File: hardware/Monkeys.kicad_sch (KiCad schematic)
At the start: 141 parts, among them IC1 SI4702-C19-GM, J1 JTAG, J2 3.3vSerial, J3 Therm, J4 PJ-320D-4A, J5 10118194-0001LF, Q1 BSS138, Q2 SI2302, Q3 MMBT3904, Q4 MMBT3904, Q5 MMBT3904, Q6 MMBT3904, SW1 SW_Push, SW2 SW_Push, SW3 SW_Push, SW4 SW_Push, SW5 SPDT_Switch_Grounded, U1 BQ24072RGT, U2 RT9080-33GJ5, U3 CH340C, U4 LM4808, U5 InfraredReceiver, U6 ESP32-WROOM-32E(8MB), Y1 32.768KHZ, Y2 32.768KHZ

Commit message: hardware: Badge revision 3.4
After a holiday break work on revision 3.4 of the Monkey badge began
March 24th, 2023.

In this revision changes were made to the following components:
- power regulator
- Charge/powerpath controller
- the headphone jack
- Resistor/capacitor values on the LM4808 amplifer
- Removal of experimental touch pads

This spin of the hardware went to initial manufacturing with the gerbers
provided on July 25th, 2023.
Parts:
- removed C13: 10uF, monkeys20221112:C_0603_1608Metric, symbol Device:C_Small
- removed CT1, CT2, CT3, CT4: Touchpad, JTFooties:CAPSENSE-CIRCLE-D10MM, symbol JTFooties2:Touchpad
- removed JP1: RESET, monkeys20221112:SolderJumper-2_P1.3mm_Open_RoundedPad1.0x1.5mm, symbol Jumper:SolderJumper_2_Open
- removed JP4: RBypassA, monkeys20221112:SolderJumper-3_P1.3mm_Bridged12_RoundedPad1.0x1.5mm, symbol Jumper:SolderJumper_3_Bridged12
- removed JP5: LBypass2, monkeys20221112:SolderJumper-3_P1.3mm_Bridged12_RoundedPad1.0x1.5mm, symbol Jumper:SolderJumper_3_Bridged12
- removed JP6: RBypassB, monkeys20221112:SolderJumper-3_P1.3mm_Bridged12_RoundedPad1.0x1.5mm, symbol Jumper:SolderJumper_3_Bridged12
- removed JP7: Amp Power Disable, monkeys20221112:SolderJumper-2_P1.3mm_Bridged_RoundedPad1.0x1.5mm, symbol Jumper:SolderJumper_2_Bridged
- added C10: 10uF, monkeys20221112:C_0603_1608Metric, symbol Device:C_Small
- added C11: 100uF, monkeys20221112:CP_EIA-6032-20_AVX-F, symbol Device:C_Polarized_Small
- added C13, C16: 330uF, Capacitor_Tantalum_SMD:CP_EIA-7343-31_Kemet-D, symbol Device:C_Polarized
- added D12: Green, monkeys20221112:LED_0805_2012Metric, symbol Device:LED
- added FB1, FB2: SCBG100505U801T, Inductor_SMD:L_0402_1005Metric, symbol Device:FerriteBead_Small
- added JP1: EXT Therm, Jumper:SolderJumper-2_P1.3mm_Bridged_RoundedPad1.0x1.5mm, symbol Jumper:SolderJumper_2_Bridged
- added JP2: ANT/GNDA, Jumper:SolderJumper-3_P1.3mm_Bridged12_RoundedPad1.0x1.5mm, symbol Jumper:SolderJumper_3_Bridged12
- added L4: 22uH, Inductor_SMD:L_Bourns-SRN4018, symbol Device:L_Ferrite
- added R37: 10K, monkeys20221112:R_0402_1005Metric, symbol Device:R_Small
- added SW6: SW_MEC_5E, JTFooties:Button_metal, symbol Switch:SW_MEC_5E
- added SW7: SPDT_Switch, monkeys20221112:SPDT Switch MSK12C02-HB, symbol JTFooties2:SPDT_Switch_Grounded
- added U7: Boost5V, Package_TO_SOT_SMD:SOT-23-5, symbol JTFooties2:ME2188C33M5
- AE1, AE2, BT2, DRA1, H1, H2, HS1, J1, J2, J3, JP12, JP13, JP14, JP15, R25, R32, R35, SAO1, SAO2, TP1: JLCPCB Part #（optional) (none) -> DNP
- BT1: footprint monkeys20221112:1xAA -> JTFooties:1xAA_NUB; JLCPCB Part #（optional) (none) -> DNP
- C15: value 10uF -> 100pF; footprint monkeys20221112:C_0603_1608Metric -> Capacitor_SMD:C_0402_1005Metric; JLCPCB Part #（optional) C326057 -> C1546; Manufacturer_Part_Number CC0603KRX5R6BB106 -> 0402CG101J500NT; SeeedSKU 302010103 -> (none); price .02 -> (none)
- C29, C30: JLCPCB Part #（optional) C109462 -> C2835558; Manufacturer_Part_Number CC0805MKX5R5BB226 -> C0805X6S226M6R3NT
- C8, C9: value 1uF -> 390nF; JLCPCB Part #（optional) C106254 -> C350937; Manufacturer_Part_Number CC0402KRX5R6BB105 -> GRM155R61A394KE15D
- D11: JLCPCB Part #（optional) C73929 -> C2764887; Manufacturer_Part_Number IR26-21C/L110/TR8 -> MHT153IRCT
- JP10: value MIC/GND -> MIC/GNDA; JLCPCB Part #（optional) (none) -> DNP
- JP3: value LBypass1 -> PWMLOUT; JLCPCB Part #（optional) (none) -> DNP
- JP9: value GND/MIC -> GNDA/MIC; JLCPCB Part #（optional) (none) -> DNP
- L1: JLCPCB Part #（optional) C408752 -> C341697; Manufacturer_Part_Number SDWL1608CR12JSTFM01 -> LQW18ANR12J00D
- LCD1: footprint monkeys20221112:PinHeader_1x04_P2.54mm_Vertical -> Connector_PinHeader_2.54mm:PinHeader_1x04_P2.54mm_Vertical; JLCPCB Part #（optional) (none) -> DNP
- R14, R16: value 3.9K -> 20K; JLCPCB Part #（optional) C51721 -> C25765; Manufacturer_Part_Number 0402WGF3901TCE -> 0402WGF2002TCE
- R17, R18: value 3.9K -> 30K; JLCPCB Part #（optional) C51721 -> C138008; Manufacturer_Part_Number 0402WGF3901TCE -> RC0402FR-0730KL
- R5: value 46.4K -> 1K; footprint monkeys20221112:R_0402_1005Metric -> monkeys20221112:R_0805_2012Metric; JLCPCB Part #（optional) C227093 -> C100046; Manufacturer_Part_Number AC0402FR-0746K4L -> RC0805JR-071KL; SeeedSKU AC0402FR-0746K4L -> 301010311
- SW5: value SPDT_Switch_Grounded -> SPDT_Switch
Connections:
- net LBP is gone; now on net PWMLOUT: JP3.3 (B)
- net +3V3: now also JP12.3 (B), JP13.1 (A), R5.2; no longer JP12.1 (A), JP13.3 (B)
- net +VDC: now also SW7.2; no longer R4.2, R6.2, U1.5 (EN2)
- net BATT: now also R32.1 (A)
- net GND: now also JP12.1 (A), JP13.3 (B), U1.14 (TMR), C10.1, C11.2, D12.1 (K), R37.1, SW6.1, SW6.2, SW7.4, U7.4 (GND); no longer JP12.3 (B), JP13.1 (A), R5.1
- net GNDA: now also JP2.3 (B); no longer JP10.1 (A), JP9.3 (B)
- net LAUD: now also C13.2, FB2.2
- net MIC: now also JP10.1 (A), JP9.3 (B); no longer JP10.3 (B), JP9.1 (A)
- net RAUD: now also C16.2, FB1.1; no longer C15.2
- net ROUT: now also C9.2
- net RST: now also SW6.3 (K), SW6.4 (A)
- net THERM: now also JP1.1 (A)
- net +5V: now reaches C7.2, R23.1, U4.8 (V+)
- net +5V: now also C11.1, U7.1 (CE), U7.2 (VOUT)
- net at R11.2, R17.1, U4.7: now also C13.1
- net at J4.R1: now also FB1.2
- net at J4.T: now also FB2.1
- net FMIP: now reaches AE1.1 (A), IC1.2 (FMIP), L1.2, TP1.1
- net FMIP: now also C15.1
- net at R15.2, R18.1, U4.1: now also C16.1; no longer C15.1
- net IO26_INFRARCV renamed PWMLOUT
- net POUT renamed OUT
- net OUT: now also R4.2, R6.2, U1.5 (EN2); no longer R32.1 (A)
- new net: D12.2 (A), R5.1
- new net: JP10.3 (B), JP2.2 (C), JP9.1 (A)
- new net: L4.1, SW7.1 (ON)
- new net: C10.2, L4.2, U7.5 (LX)
- new net: C15.2, JP2.1 (A)
- new net: JP1.2 (B), R37.2
- no-connect marks 24 -> 25
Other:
- note added: "Cb"
- note added: "Charge, Powerpath Coontroller & On/Off Switch"
- note added: "Ci"
- note added: "Co"
- note added: "Cs"
- note added: "Cut if using ext therm"
- note added: "External NTC 10k 1% Thermistor on battery"
- note added: "Rf"
- note added: "Ri"
- note added: "https://www.alibaba.com/product-detail/14500-Rechargeable-Battery-AA-2800mAh-3_1600779695589.html?spm=a2700.galleryofferlist.normal_offer.d_title.a7ed2679IqySss"
- note added: "https://www.alibaba.com/product-detail/Gaonengmax-3-7V-14500-1200mah-li_1600451606725.html?spm=a2700.galleryofferlist.normal_offer.d_title.1a322679m4llBO"
- note added: "https://www.alibaba.com/product-detail/Rechargeable-Cylinder-14500-1200mAh-Lithium-Battery_1600453629274.html?spm=a2700.galleryofferlist.normal_offer.d_title.1a322679m4llBO"
- note removed: "32mA"
- note removed: "46.4K R5 = 6.25Hr Limit on charge"
- note removed: "Charge & Powerpath Controller"
- note removed: "Experimental Alternative to physical buttons"
- note removed: "External 10k 1% Thermistor on battery"
- note removed: "two 1UF caps in series, close enough to 2.2uF"
- moved on the sheet: C27, D10, D9, JP10, JP12, JP13, JP14, JP15, JP9, R17, R18, R4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

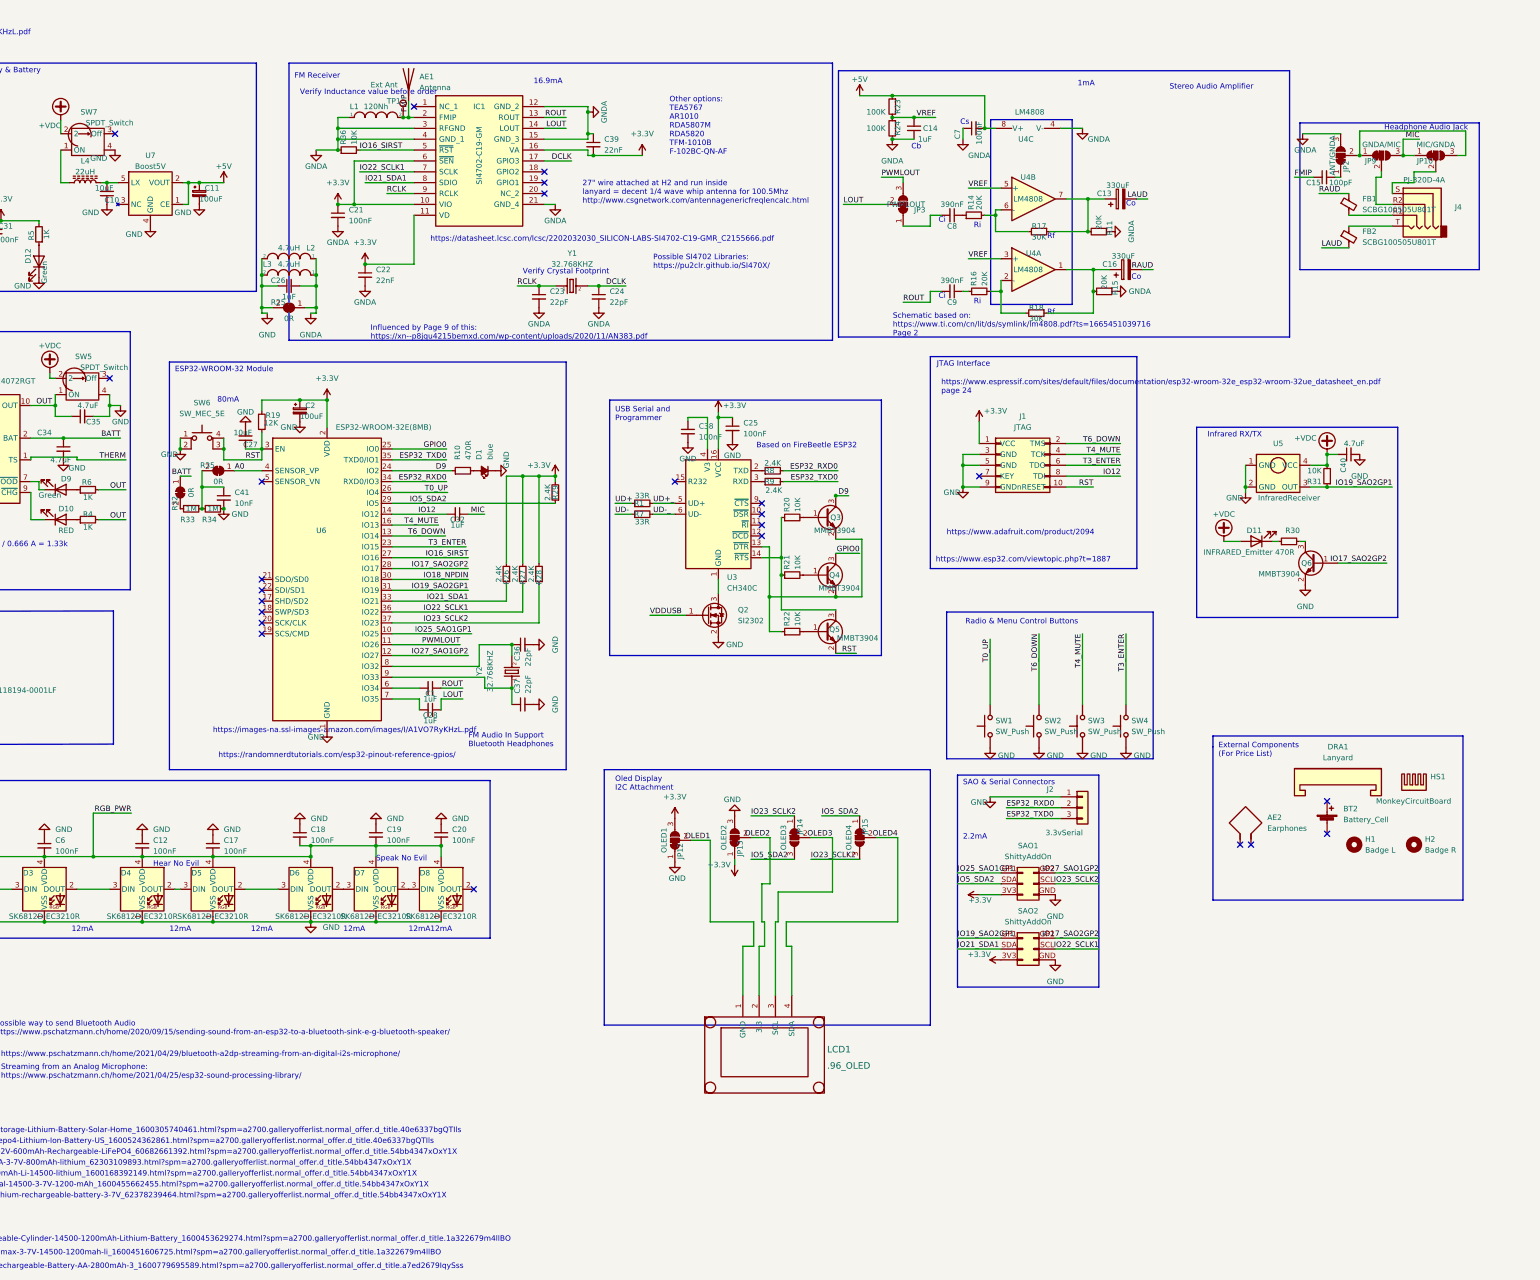
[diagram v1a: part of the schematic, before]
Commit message: hardware: Badge revision 3.5
In this revision changes were made to the following components:

- Stereo amplifier
- Microphone amplifier
- Addition of a JTAG port

This spin of the hardware went to initial manufacturing with the gerbers
provided on August 30th, 2023.
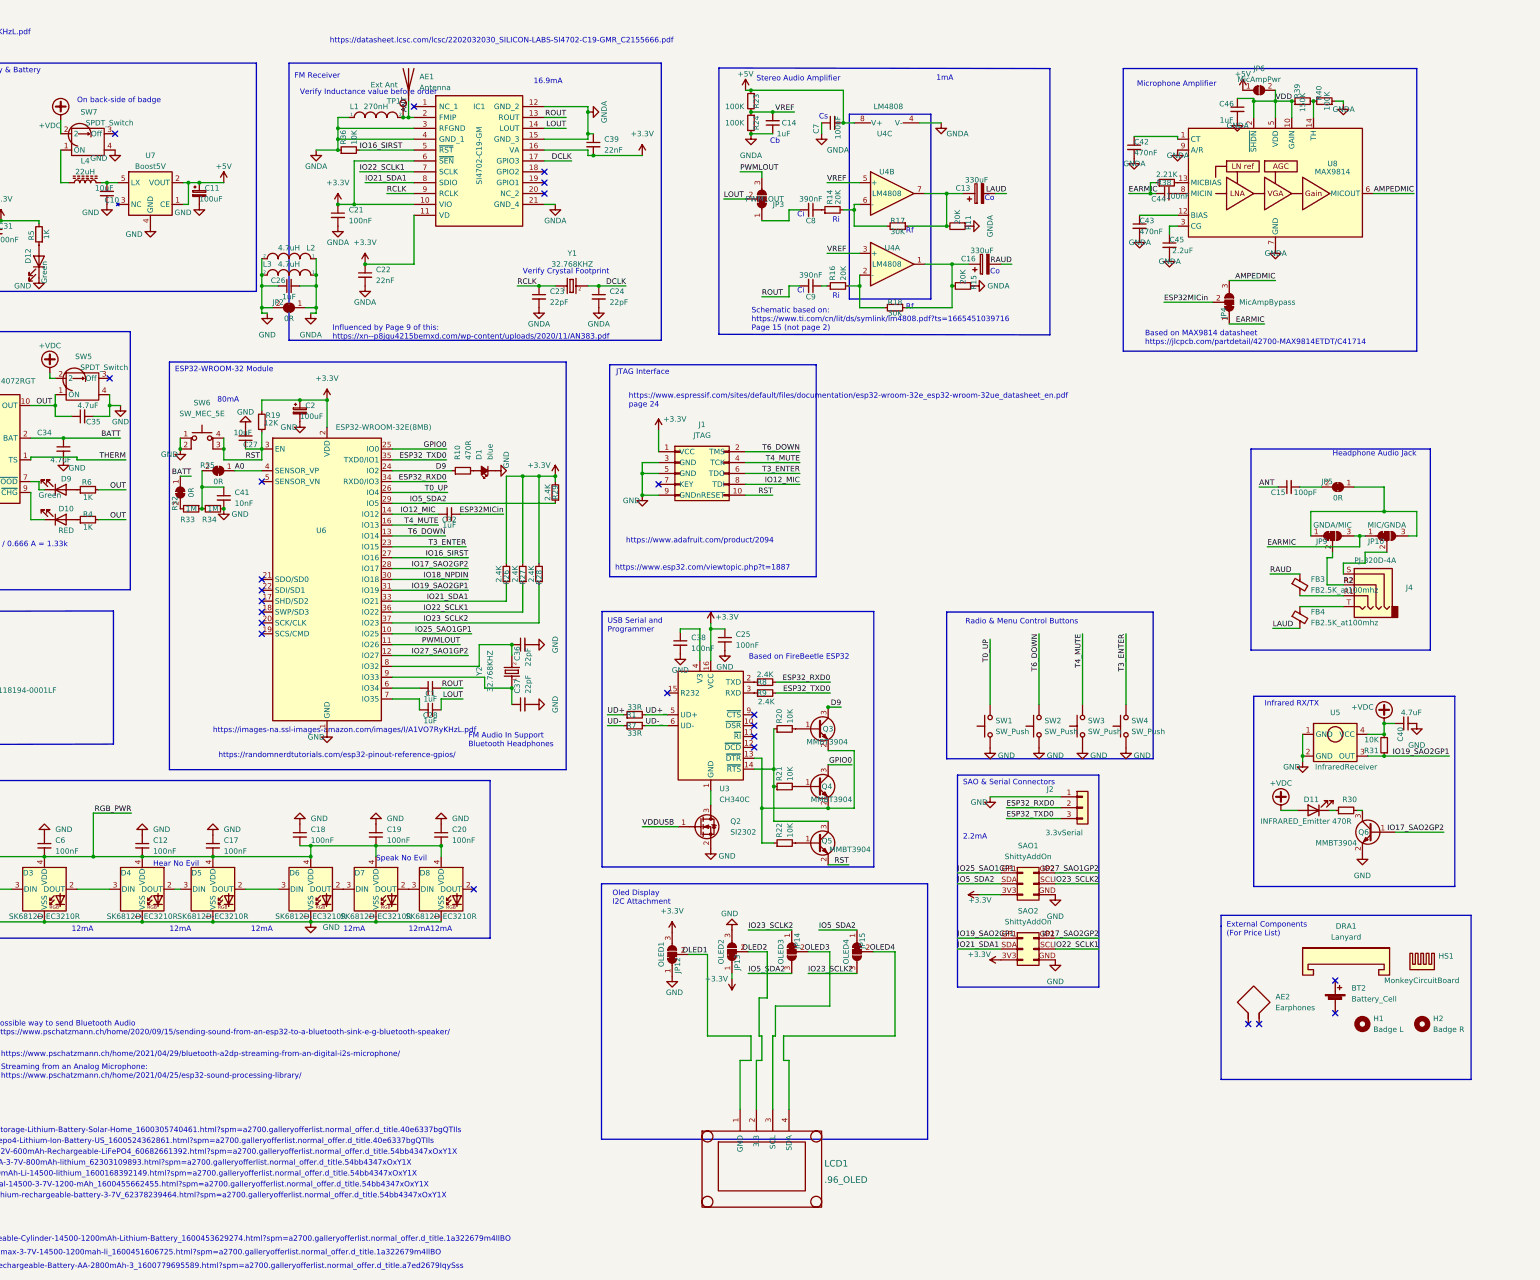
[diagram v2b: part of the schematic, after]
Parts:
- removed FB1, FB2: SCBG100505U801T, Inductor_SMD:L_0402_1005Metric, symbol Device:FerriteBead_Small
- removed JP2: ANT/GNDA, Jumper:SolderJumper-3_P1.3mm_Bridged12_RoundedPad1.0x1.5mm, symbol Jumper:SolderJumper_3_Bridged12
- added C42, C43: 470nF, monkeys20221112:C_0402_1005Metric, symbol Device:C_Small
- added C44: 100nF, monkeys20221112:C_0402_1005Metric, symbol Device:C_Small
- added C45: 2.2uF, monkeys20221112:C_0402_1005Metric, symbol Device:C_Small
- added C46: 1uF, monkeys20221112:C_0402_1005Metric, symbol Device:C_Small
- added FB3, FB4: FB2.5K_at100mhz, Capacitor_SMD:C_0603_1608Metric, symbol Device:FerriteBead_Small
- added JP4: MicAmpBypass, monkeys20221112:SolderJumper-3_P1.3mm_Bridged12_RoundedPad1.0x1.5mm, symbol Jumper:SolderJumper_3_Bridged12
- added JP5: 0R, monkeys20221112:SolderJumper-2_P1.3mm_Bridged_RoundedPad1.0x1.5mm, symbol Jumper:SolderJumper_2_Bridged
- added JP6: MicAmpPwr, Jumper:SolderJumper-2_P1.3mm_Open_RoundedPad1.0x1.5mm, symbol Jumper:SolderJumper_2_Open
- added R38: 2.21K, monkeys20221112:R_0402_1005Metric, symbol Device:R_Small
- added R39: 150K, monkeys20221112:R_0402_1005Metric, symbol Device:R_Small
- added R40: 100K, monkeys20221112:R_0402_1005Metric, symbol Device:R_Small
- added U8: MAX9814, Package_DFN_QFN:DFN-14-1EP_3x3mm_P0.4mm_EP1.78x2.35mm, symbol JTFooties2:MAX9814
- C8, C9: footprint monkeys20221112:C_0402_1005Metric -> monkeys20221112:C_0805_2012Metric; JLCPCB Part #（optional) C350937 -> C327132; Manufacturer_Part_Number GRM155R61A394KE15D -> CC0805KKX7R7BB394
- L1: value 120Nh -> 270nH; JLCPCB Part #（optional) C341697 -> C578010; Manufacturer_Part_Number LQW18ANR12J00D -> SCHF160808HR27JT; price .05 -> (none)
- renumbered R25 to JP2
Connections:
- net +5V: now also JP6.1 (A)
- net GNDA: now also C42.2, C43.2, C45.2, C46.2, R40.1, U8.11 (GND), U8.15 (GND), U8.4 (GND), U8.7 (GND), U8.9 (A/R)
- net LAUD: now also FB4.2
- net RAUD: now also FB3.1
- net at JP10.3 (B), JP9.1 (A): now also JP5.1 (A)
- net at J4.R1: now also FB3.2
- net R2: now reaches J4.R2, JP9.2 (C)
- net at J4.T: now also FB4.1
- net at C15.2: now also JP5.2 (B)
- net FMIP renamed ANT
- net IO12 renamed IO12_MIC
- net MIC renamed EARMIC
- net EARMIC: now also C44.1, JP4.1 (A), R38.1; no longer C32.1
- new net: R38.2, U8.13 (MICBIAS)
- new net: C44.2, U8.8 (MICIN)
- new net: C45.1, U8.3 (CG)
- new net: C42.1, U8.1 (CT)
- new net: R39.2, R40.2, U8.14 (TH)
- new net: C43.1, U8.12 (BIAS)
- new net AMPEDMIC: JP4.3 (B), U8.6 (MICOUT)
- new net ESP32MICin: C32.1, JP4.2 (C)
- new net VDD: C46.1, JP6.2 (B), R39.1, U8.10 (GAIN), U8.2 (~{SHDN}), U8.5 (VDD)
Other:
- note added: "Based on MAX9814 datasheet https://jlcpcb.com/partdetail/42700-MAX9814ETDT/C41714"
- note added: "Microphone Amplifier"
- note added: "On back-side of badge"
- note added: "Schematic based on: https://www.ti.com/cn/lit/ds/symlink/lm4808.pdf?ts=1665451039716 Page 15 (not page 2)"
- note removed: "27" wire attached at H2 and run inside lanyard = decent 1/4 wave whip antenna for 100.5Mhz http://www.csgnetwork.com/antennagenericfreqlencalc.html"
- note removed: "Other options: TEA5767 AR1010 RDA5807M RDA5820 TFM-1010B F-102BC-QN-AF"
- note removed: "Possible SI4702 Libraries: https://pu2clr.github.io/SI470X/"
- note removed: "Schematic based on: https://www.ti.com/cn/lit/ds/symlink/lm4808.pdf?ts=1665451039716 Page 2"
- moved on the sheet: AE2, BT2, C13, C14, C15, C16, C25, C32, C38, C40, C7, C8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
